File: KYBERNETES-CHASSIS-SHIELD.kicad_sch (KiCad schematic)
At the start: 29 parts, among them J1 ESC, J2 Radio, J3 Encoder, J4 I2C, J5 Servo 1, J6 Servo 2, J7 Servo Regulator 1, J8 Servo Regulator 2, U1 LM4040CEM3-3.0T, U2 LM2903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

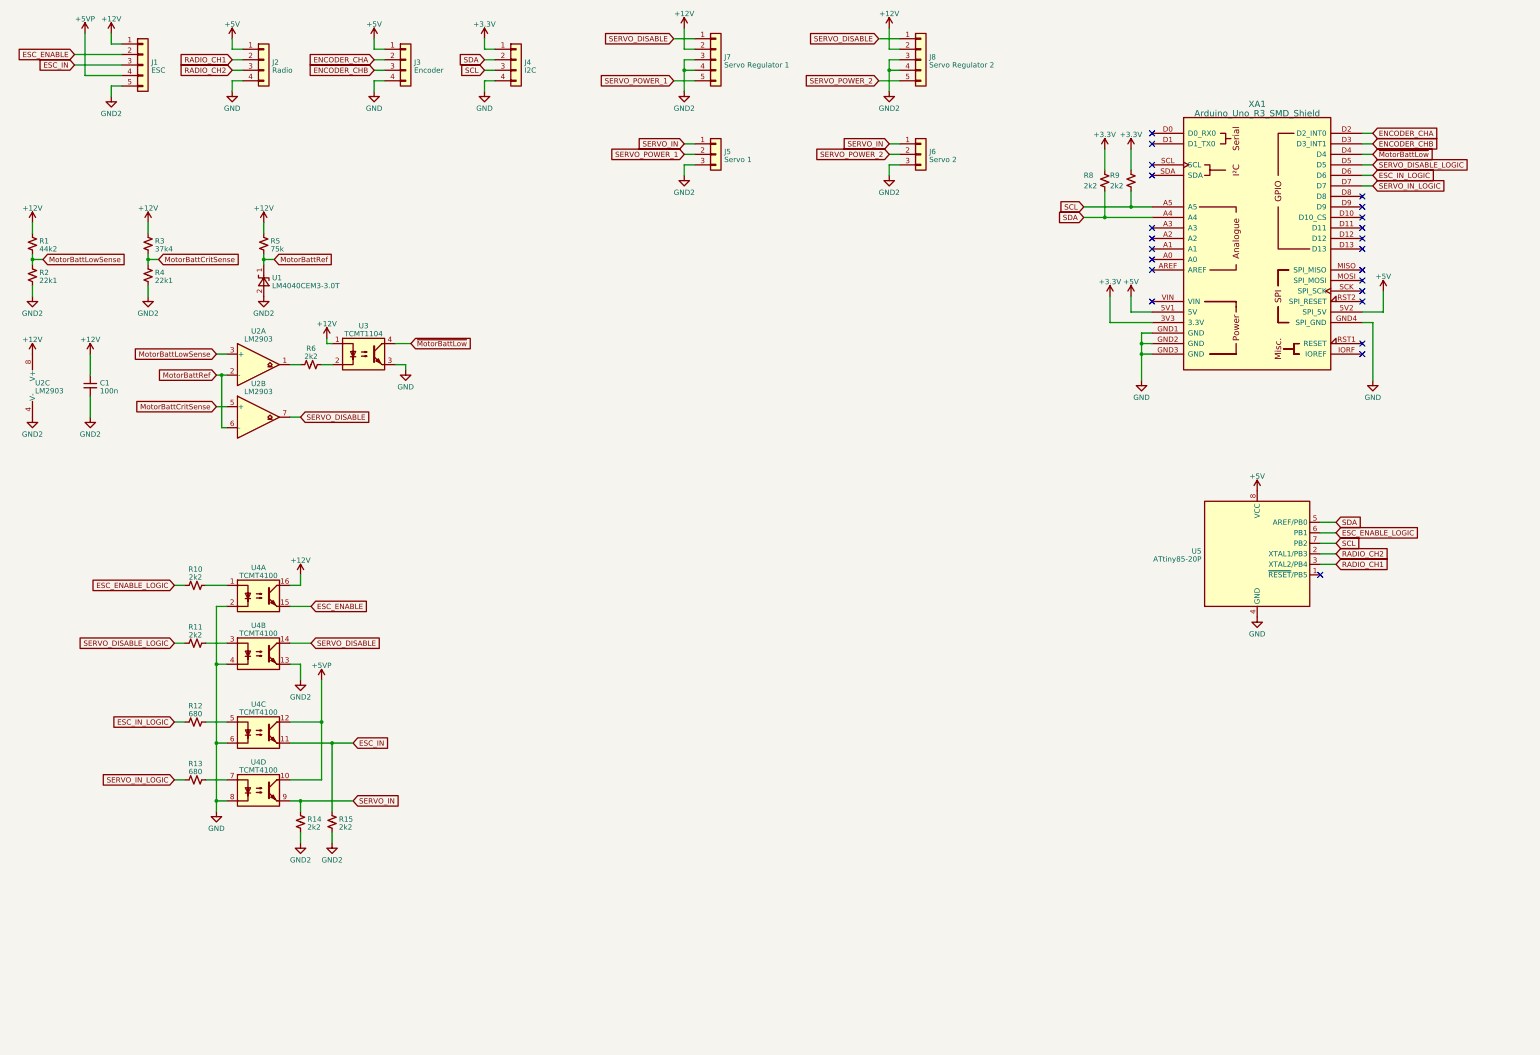
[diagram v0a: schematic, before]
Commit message: rework into 4 layer board
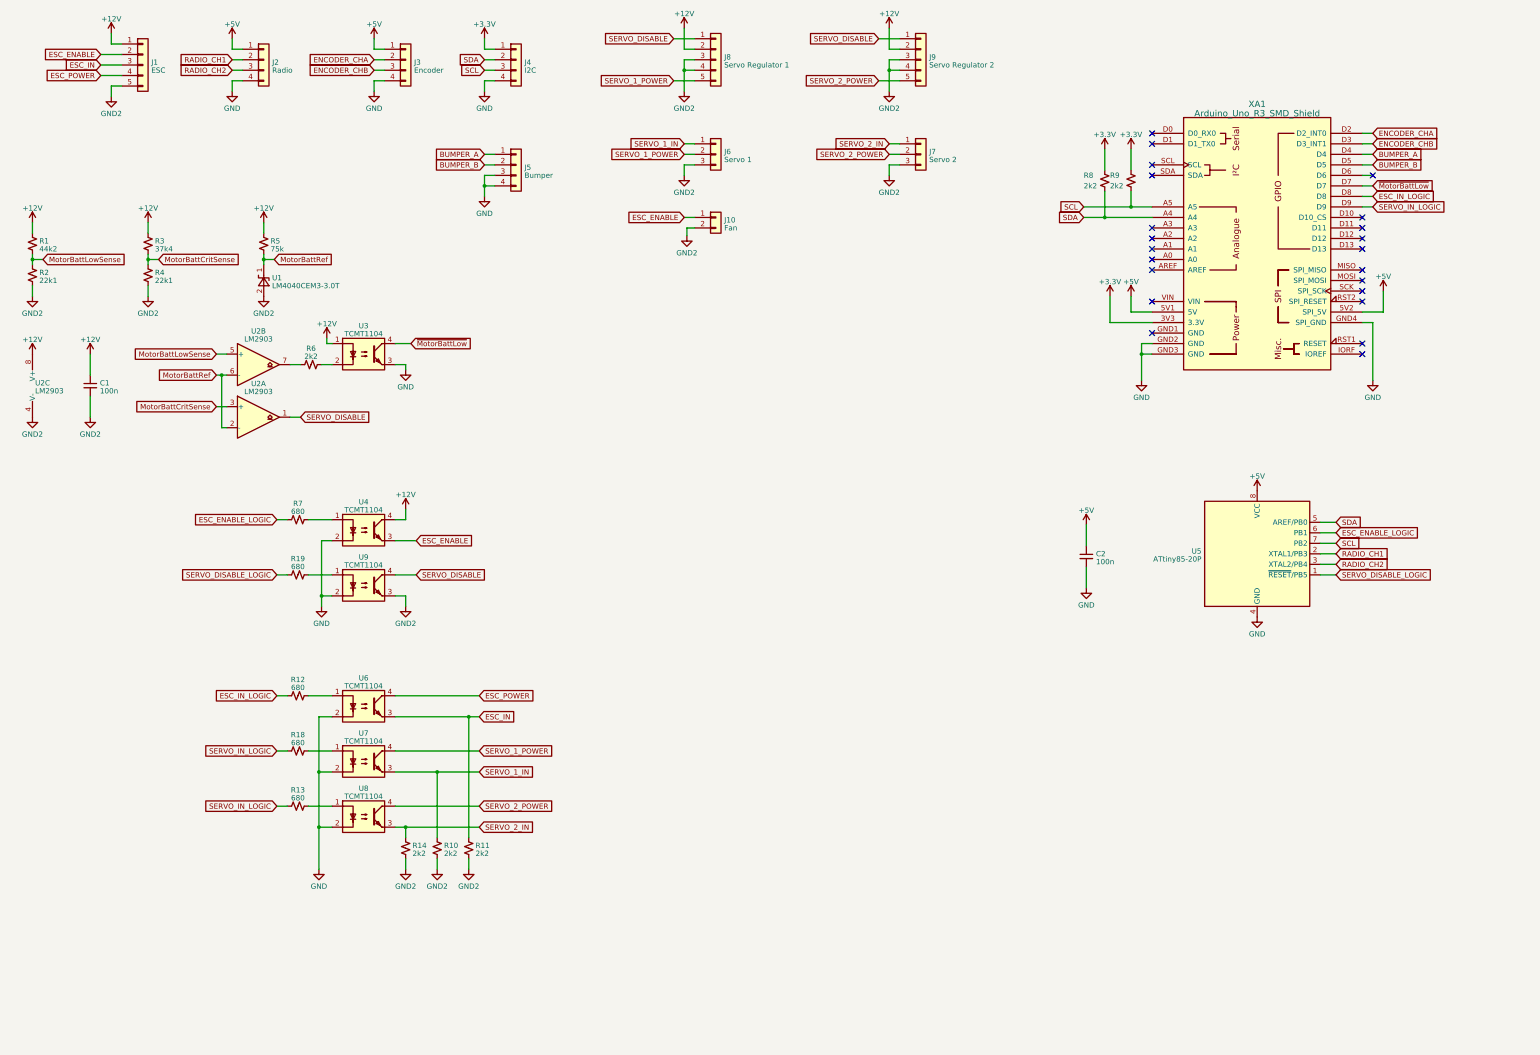
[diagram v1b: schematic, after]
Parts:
- removed R15: 2k2, Resistor_SMD:R_0603_1608Metric_Pad0.98x0.95mm_HandSolder, symbol Device:R_Small_US
- removed U4: TCMT4100, Package_SO:SOP-16_4.4x10.4mm_P1.27mm, symbol Isolator:TCMT4100
- added C2: 100n, Capacitor_SMD:C_0603_1608Metric_Pad1.08x0.95mm_HandSolder, symbol Device:C_Small
- added J10: Fan, Connector_JST:JST_PH_B2B-PH-K_1x02_P2.00mm_Vertical, symbol Connector_Generic:Conn_01x02
- added J5: Bumper, Connector_JST:JST_PH_B4B-PH-K_1x04_P2.00mm_Vertical, symbol Connector_Generic:Conn_01x04
- added R10: 2k2, Resistor_SMD:R_0603_1608Metric_Pad0.98x0.95mm_HandSolder, symbol Device:R_Small_US
- added R18, R19: 680, Resistor_SMD:R_0603_1608Metric_Pad0.98x0.95mm_HandSolder, symbol Device:R_Small_US
- added U4, U6, U7, U8, U9: TCMT1104, Package_SO:SOP-4_4.4x2.6mm_P1.27mm, symbol Isolator:TCMT1104
- C1: footprint Capacitor_SMD:C_0402_1005Metric -> Capacitor_SMD:C_0603_1608Metric_Pad1.08x0.95mm_HandSolder
- R1, R2, R3, R4, R5: footprint Resistor_SMD:R_0402_1005Metric -> Resistor_SMD:R_0603_1608Metric_Pad0.98x0.95mm_HandSolder
- R7: renamed from R10; value 2k2 -> 680
- renumbered J5 to J6, J6 to J7, J7 to J8, J8 to J9
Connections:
- net +12V: now also U4.4
- net +5V: now also C2.1
- net ESC_ENABLE: now also J10.1 (Pin_1), U4.3
- net ESC_IN: now also R11.1, U6.3
- net ESC_IN_LOGIC: now also XA1.D8; no longer XA1.D6
- net GND: now also C2.2, J5.3 (Pin_3), J5.4 (Pin_4), U4.2, U6.2, U7.2, U8.2, U9.2; no longer XA1.GND1 (GND)
- net GND2: now also R11.2, J10.2 (Pin_2), R10.2, U9.3
- net MotorBattCritSense: now also U2.3 (+); no longer U2.5 (+)
- net MotorBattLowSense: now also U2.5 (+); no longer U2.3 (+)
- net RADIO_CH1: now also U5.2 (XTAL1/PB3); no longer U5.3 (XTAL2/PB4)
- net RADIO_CH2: now also U5.3 (XTAL2/PB4); no longer U5.2 (XTAL1/PB3)
- net SERVO_DISABLE: now also U2.1, U9.4; no longer U2.7
- net SERVO_DISABLE_LOGIC: now also U5.1 (~{RESET}/PB5), R19.1; no longer R11.1, XA1.D5
- net SERVO_IN_LOGIC: now also XA1.D9, R18.1; no longer XA1.D7
- net ~{MotorBattLow}: now also XA1.D7; no longer XA1.D4
- net at R12.2: now also U6.1
- net at R7.2: now also U4.1
- net at R13.2: now also U8.1
- net at R6.1: now also U2.7; no longer U2.1
- net +5VP renamed ESC_POWER
- net ESC_POWER: now also U6.4
- net SERVO_IN renamed SERVO_2_IN
- net SERVO_2_IN: now also U8.3; no longer J6.1 (Pin_1)
- net SERVO_POWER_1 renamed SERVO_1_POWER
- net SERVO_1_POWER: now also U7.4
- net SERVO_POWER_2 renamed SERVO_2_POWER
- net SERVO_2_POWER: now also U8.4
- new net: R19.2, U9.1
- new net: R18.2, U7.1
- new net BUMPER_A: J5.1 (Pin_1), XA1.D4
- new net BUMPER_B: J5.2 (Pin_2), XA1.D5
- new net SERVO_1_IN: J6.1 (Pin_1), R10.1, U7.3
- no-connect marks 23 -> 22
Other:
- moved on the sheet: R7, U2A, U2B

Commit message: add comparator bias resistor, increase low voltage thresholds, add large capacitors for servos
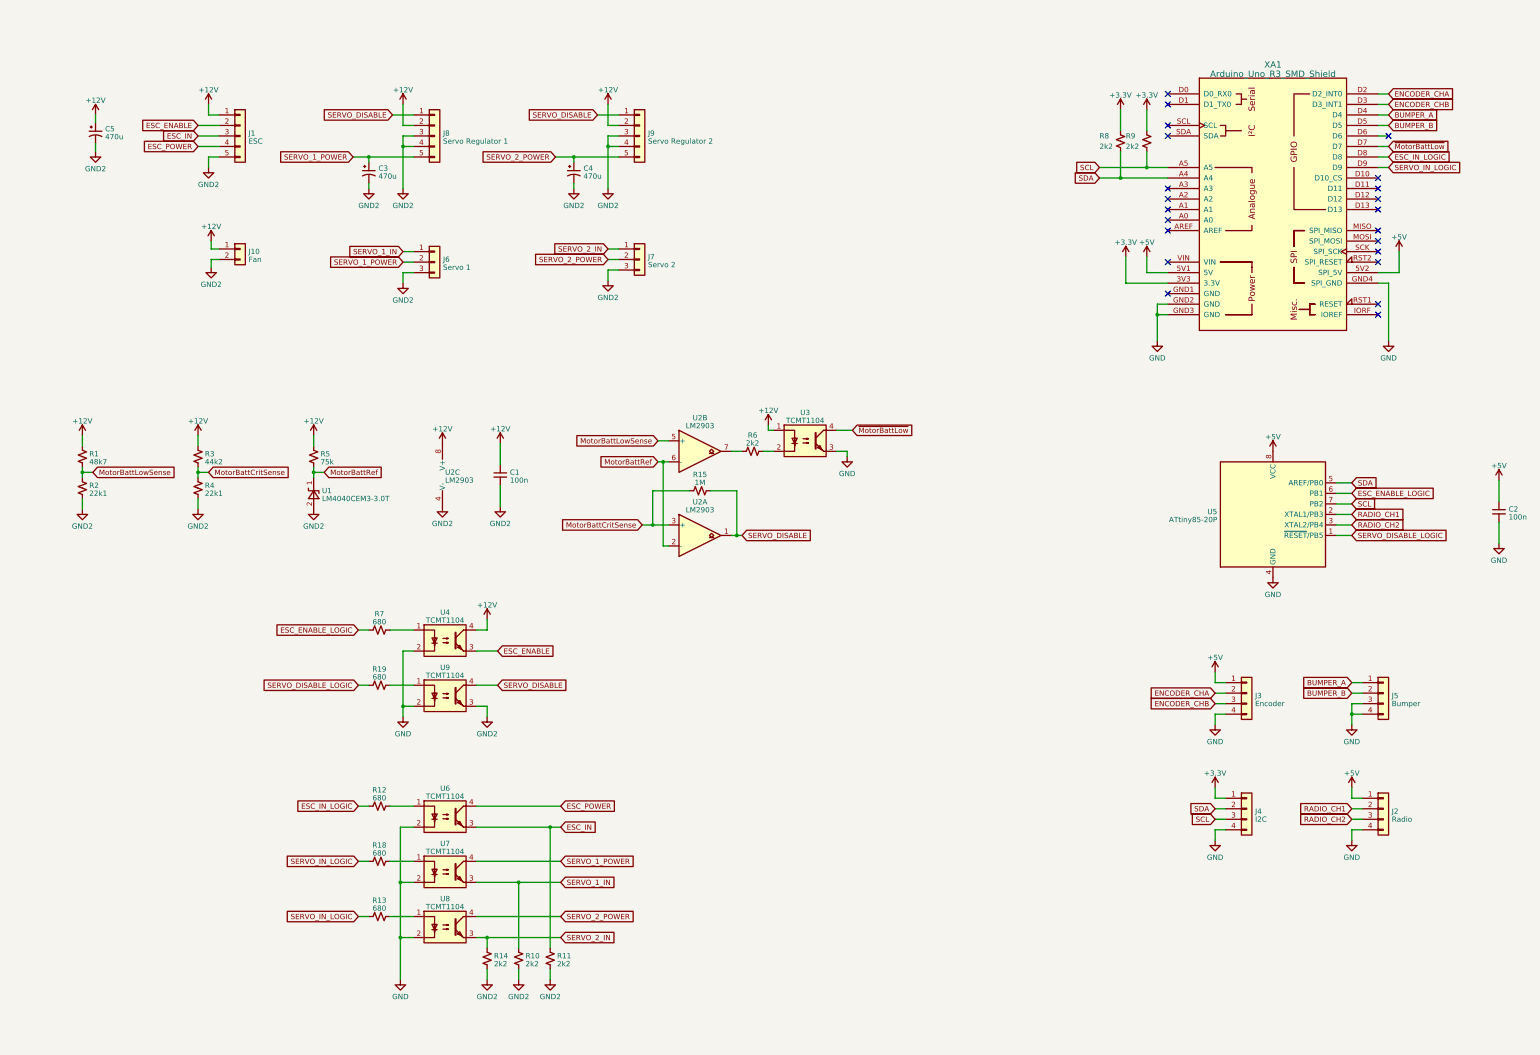
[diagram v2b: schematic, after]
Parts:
- added C3, C4, C5: 470u, Capacitor_SMD:CP_Elec_8x10, symbol Device:C_Polarized_Small_US
- added R15: 1M, Resistor_SMD:R_0603_1608Metric_Pad0.98x0.95mm_HandSolder, symbol Device:R_Small_US
- R1: value 44k2 -> 48k7
- R3: value 37k4 -> 44k2
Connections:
- net +12V: now also J10.1 (Pin_1), C5.1
- net ESC_ENABLE: no longer J10.1 (Pin_1)
- net GND2: now also C3.2, C4.2, C5.2
- net MotorBattCritSense: now also R15.1
- net SERVO_1_POWER: now also C3.1
- net SERVO_2_POWER: now also C4.1
- net SERVO_DISABLE: now also R15.2
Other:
- moved on the sheet: C1, C2, J1, J10, J2, J3, J4, J5, J6, J7, J8, J9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

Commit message: fix the incorrect footprint for desired capacitors (wurth 875115357006)
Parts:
- C3, C4, C5: footprint Capacitor_SMD:CP_Elec_8x10 -> Capacitor_SMD:CP_Elec_10x10.5
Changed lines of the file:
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@@
       (effects (font (size 1.27 1.27)) (justify left))
     )
-    (property "Footprint" "Capacitor_SMD:CP_Elec_8x10" (at 158.75 65.405 0)
+    (property "Footprint" "Capacitor_SMD:CP_Elec_10x10.5" (at 158.75 65.405 0)
       (effects (font (size 1.27 1.27)) hide)
     )
@@
       (effects (font (size 1.27 1.27)) (justify left))
     )
-    (property "Footprint" "Capacitor_SMD:CP_Elec_8x10" (at 43.18 55.88 0)
+    (property "Footprint" "Capacitor_SMD:CP_Elec_10x10.5" (at 43.18 55.88 0)
       (effects (font (size 1.27 1.27)) hide)
     )
@@
       (effects (font (size 1.27 1.27)) (justify left))
     )
-    (property "Footprint" "Capacitor_SMD:CP_Elec_8x10" (at 109.22 65.405 0)
-      (effects (font (size 1.27 1.27)) hide)
-    )
+    (property "Footprint" "Capacitor_SMD:CP_Elec_10x10.5" (at 109.22 65.405 0)
+      (effects (font (size 1.27 1.27)) hide)
+    )
